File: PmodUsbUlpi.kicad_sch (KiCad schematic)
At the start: 17 parts, among them J1 USB_C_Receptacle_USB2.0, J2 2x10 Header, U1 TPS76318, U2 USB3320

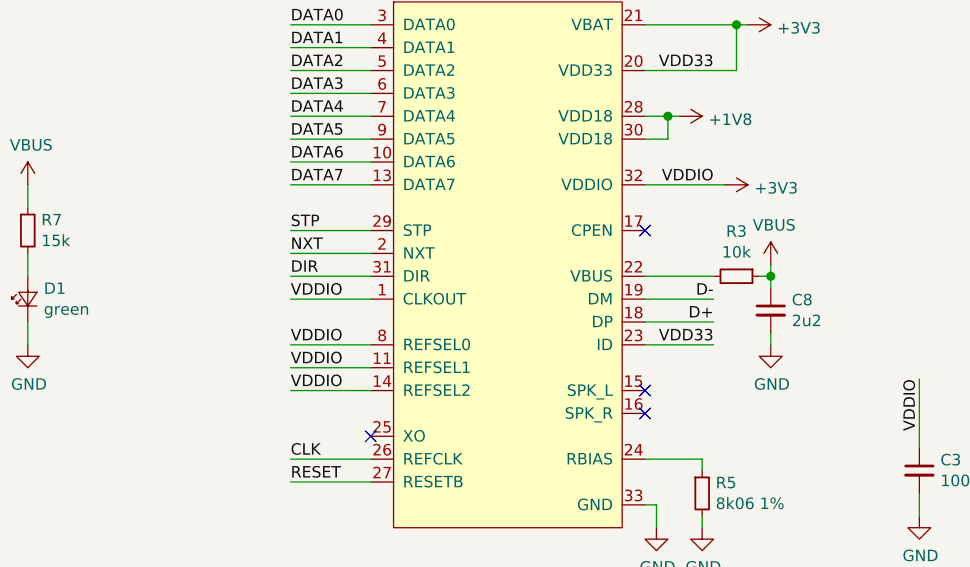
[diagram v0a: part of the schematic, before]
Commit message: first version with 1.8V
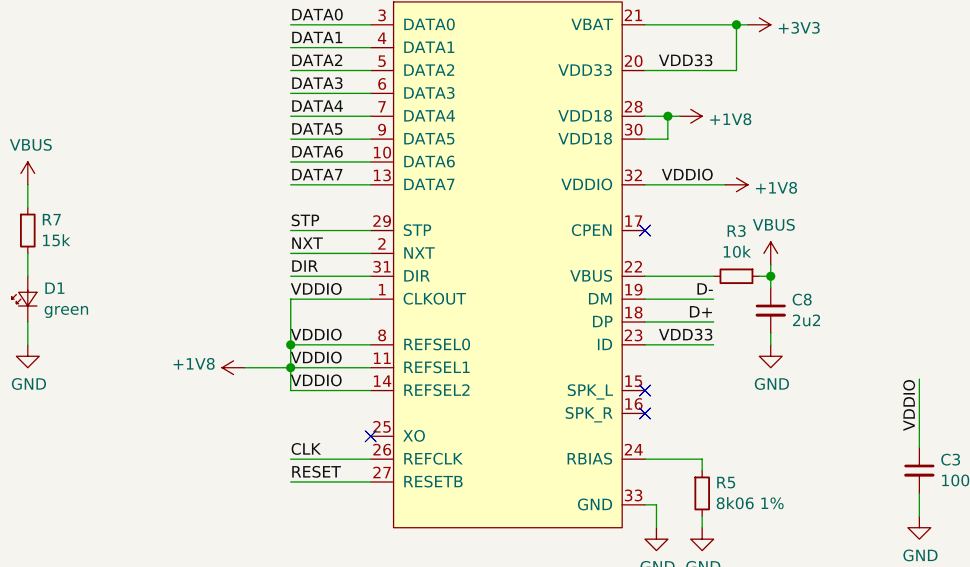
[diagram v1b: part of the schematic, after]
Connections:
- net +1V8: now also C3.1, U2.1 (CLKOUT), U2.11 (REFSEL1), U2.14 (REFSEL2), U2.32 (VDDIO), U2.8 (REFSEL0)
- net +3V3: no longer C3.1, U2.1 (CLKOUT), U2.11 (REFSEL1), U2.14 (REFSEL2), U2.32 (VDDIO), U2.8 (REFSEL0)
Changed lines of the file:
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@@
-(kicad_sch (version 20210406) (generator eeschema)
+(kicad_sch (version 20210621) (generator eeschema)
   (paper "A4")
   (title_block
@@
   (junction (at 149.86 107.95) (diameter 1.016) (color 0 0 0 0))
   (junction (at 158.75 97.79) (diameter 1.016) (color 0 0 0 0))
+  (junction (at 194.31 59.69) (diameter 1.016) (color 0 0 0 0))
+  (junction (at 194.31 62.23) (diameter 1.016) (color 0 0 0 0))
   (junction (at 236.22 34.29) (diameter 1.016) (color 0 0 0 0))
   (junction (at 243.84 24.13) (diameter 1.016) (color 0 0 0 0))
@@
     (stroke (width 0) (type solid) (color 0 0 0 0))
   )
+  (wire (pts (xy 189.23 62.23) (xy 194.31 62.23))
+    (stroke (width 0) (type solid) (color 0 0 0 0))
+  )
   (wire (pts (xy 190.5 128.27) (xy 190.5 113.03))
     (stroke (width 0) (type solid) (color 0 0 0 0))
@@
     (stroke (width 0) (type solid) (color 0 0 0 0))
   )
+  (wire (pts (xy 194.31 54.61) (xy 194.31 59.69))
+    (stroke (width 0) (type solid) (color 0 0 0 0))
+  )
   (wire (pts (xy 194.31 54.61) (xy 203.2 54.61))
     (stroke (width 0) (type solid) (color 0 0 0 0))
   )
+  (wire (pts (xy 194.31 59.69) (xy 194.31 62.23))
+    (stroke (width 0) (type solid) (color 0 0 0 0))
+  )
   (wire (pts (xy 194.31 59.69) (xy 203.2 59.69))
+    (stroke (width 0) (type solid) (color 0 0 0 0))
+  )
+  (wire (pts (xy 194.31 62.23) (xy 194.31 64.77))
     (stroke (width 0) (type solid) (color 0 0 0 0))
   )
@@
     (pin "1")
   )
+  (symbol (lib_id "power:+1V8") (at 189.23 62.23 90) (unit 1)
+    (in_bom yes) (on_board yes)
+    (property "Reference" "#PWR?" (id 0) (at 193.04 62.23 0)
+      (effects (font (size 1.27 1.27)) hide)
+    )
+    (property "Value" "+1V8" (id 1) (at 185.9788 61.849 90)
+      (effects (font (size 1.27 1.27)) (justify left))
+    )
+    (property "Footprint" "" (id 2) (at 189.23 62.23 0)
+      (effects (font (size 1.27 1.27)) hide)
+    )
+    (property "Datasheet" "" (id 3) (at 189.23 62.23 0)
+      (effects (font (size 1.27 1.27)) hide)
+    )
+    (pin "1")
+  )
   (symbol (lib_id "power:+3.3V") (at 190.5 113.03 0) (unit 1)
     (in_bom yes) (on_board yes)
@@
     (pin "1")
   )
-  (symbol (lib_id "power:+3V3") (at 242.57 41.91 270) (unit 1)
-    (in_bom yes) (on_board yes)
-    (property "Reference" "#PWR0124" (id 0) (at 238.76 41.91 0)
-      (effects (font (size 1.27 1.27)) hide)
-    )
-    (property "Value" "+3V3" (id 1) (at 245.8212 42.291 90)
+  (symbol (lib_id "power:+1V8") (at 242.57 41.91 270) (unit 1)
+    (in_bom yes) (on_board yes)
+    (property "Reference" "#PWR0110" (id 0) (at 238.76 41.91 0)
+      (effects (font (size 1.27 1.27)) hide)
+    )
+    (property "Value" "+1V8" (id 1) (at 245.8212 42.291 90)
       (effects (font (size 1.27 1.27)) (justify left))
     )
@@
       (reference "#PWR0109") (unit 1) (value "VBUS") (footprint "")
     )
+    (path "/d42b7ee0-eb43-4246-9d57-ee563022b036"
+      (reference "#PWR0110") (unit 1) (value "+1V8") (footprint "")
+    )
     (path "/00000000-0000-0000-0000-000060363997"
       (reference "#PWR0112") (unit 1) (value "+3.3V") (footprint "")
@@
       (reference "#PWR0123") (unit 1) (value "GND") (footprint "")
     )
-    (path "/00000000-0000-0000-0000-000060605400"
-      (reference "#PWR0124") (unit 1) (value "+3V3") (footprint "")
-    )
     (path "/00000000-0000-0000-0000-000060609659"
       (reference "#PWR0125") (unit 1) (value "+1V8") (footprint "")
@@
       (reference "#PWR0132") (unit 1) (value "GND") (footprint "")
     )
+    (path "/c26f716d-d67a-4c57-887c-c39788c0f77e"
+      (reference "#PWR?") (unit 1) (value "+1V8") (footprint "")
+    )
     (path "/00000000-0000-0000-0000-00006056f1f6"
